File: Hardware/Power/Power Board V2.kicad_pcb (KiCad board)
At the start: 2 copper layers, 71.1 x 58.4 mm, 90 parts, among them IC1 LM3481MM, IC2 BP1360, IC3 DIO6912, IC4 BP1360, IC5 DIO6912, J1 Conn_01x02, J2 Conn_01x02, J3 Conn_01x02, J4 Conn_01x02, J5 Conn_02x05_Top_Bottom, Q1 2N7000, Q2 AO4264E, Q3 2N7000, Q4 PJM2301PSA-S

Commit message: KiCad Cleanup
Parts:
- added REF**: SOIC-8_3.9x4.9mm_P1.27mm, Package_SO:SOIC-8_3.9x4.9mm_P1.27mm, B.Cu at (168.8, 91.3)
- moved R5 3.03 mm to (110.7, 90.9), turned to 135 degrees
- moved R2 2.43 mm to (110.2, 83.2), turned to 0 degrees
- moved C8 2.13 mm to (110.2, 85.0), turned to 0 degrees
- moved R1 1.33 mm to (112.0, 89.7), turned to 135 degrees
- moved R6 0.44 mm to (112.4, 94.7)
- moved R4 0.40 mm to (113.8, 84.1)
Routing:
- net Net-(IC1-Pad8): track 17.5 -> 13.8 mm
- net Net-(Q2-Pad1): track 7.12 -> 3.82 mm
- net Net-(IC1-Pad2): track 21.4 -> 24.6 mm
- net Net-(C8-Pad1): track 18.2 -> 20.3 mm
- net GNDA: track 15.7 -> 14.7 mm, vias 55 -> 61
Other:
- board text added: "1"
- board text added: "Note: Pin 1 designator is longer line over pin"

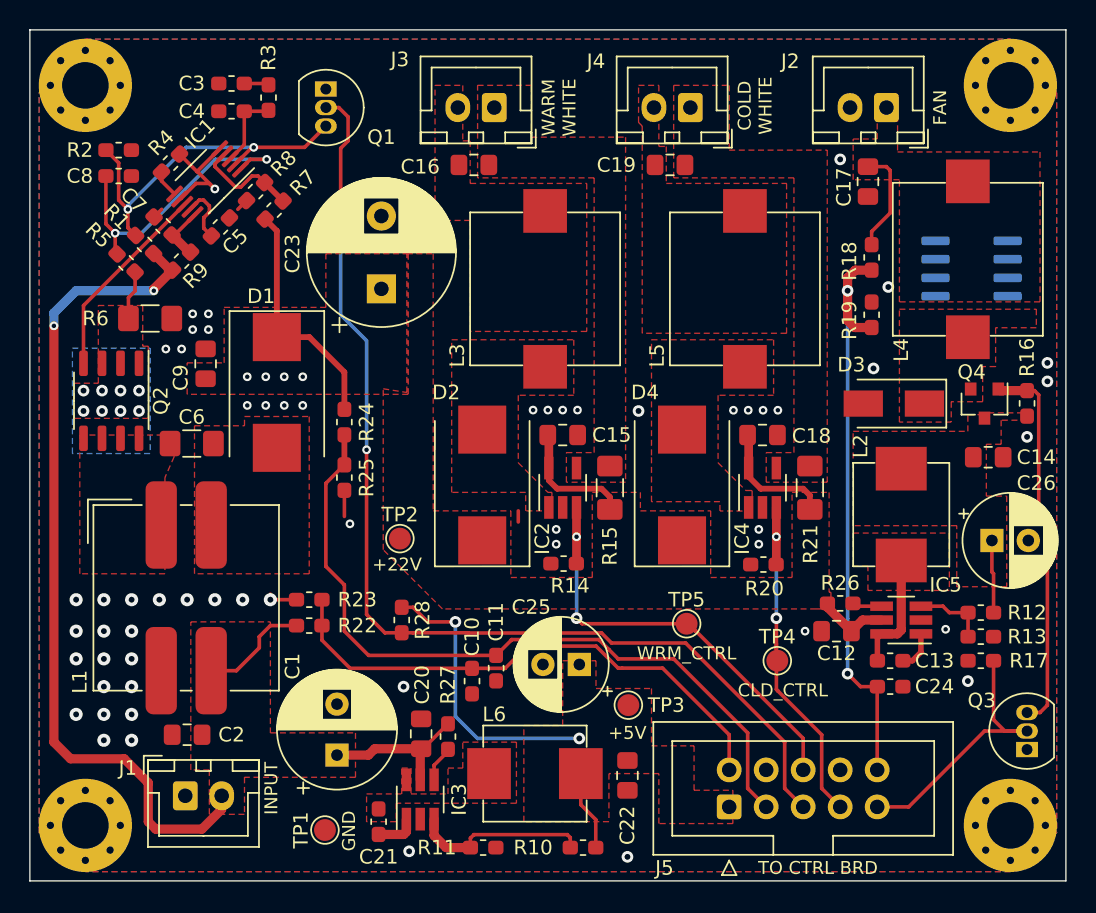
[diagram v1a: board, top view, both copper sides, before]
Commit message: Moved MCU Power Supply to Logic Board
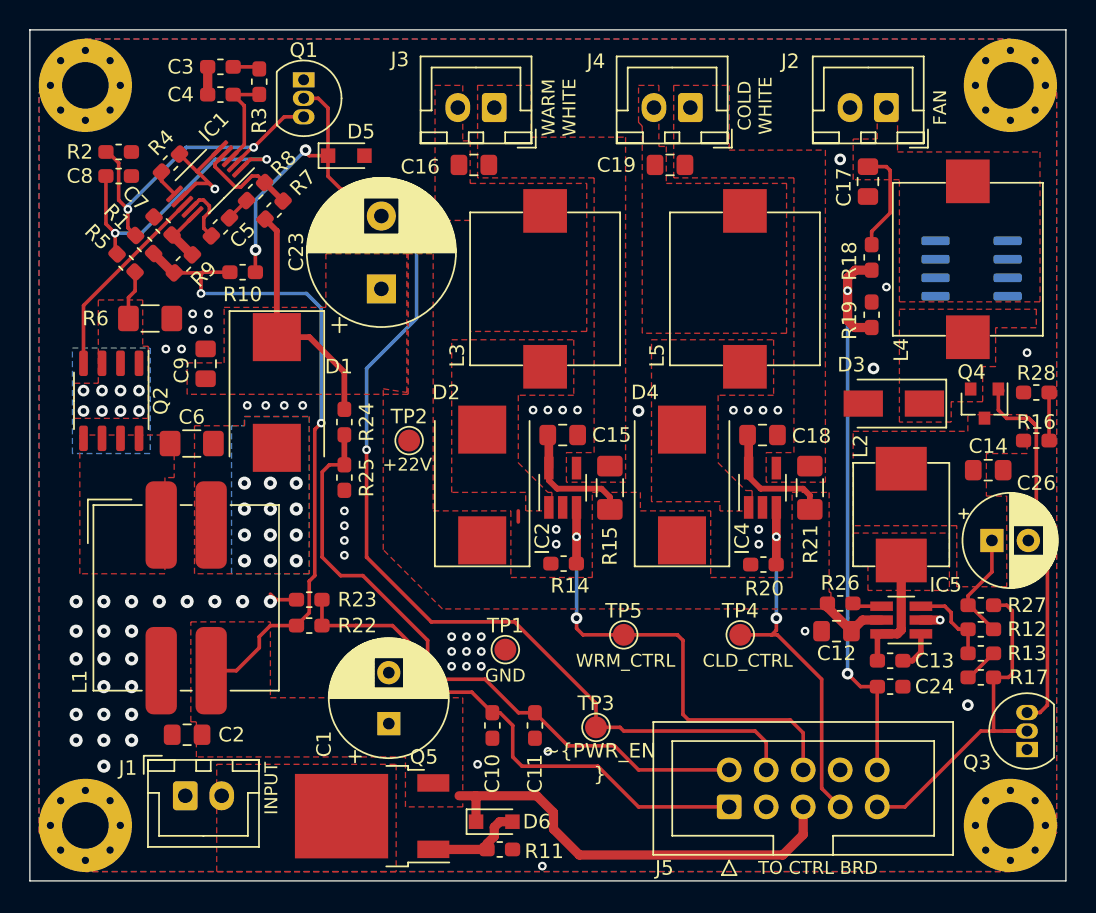
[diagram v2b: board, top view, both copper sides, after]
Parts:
- removed C20, C22: 2U2, Capacitor_SMD:C_0805_2012Metric_Pad1.15x1.40mm_HandSolder
- removed C21: 100N, Capacitor_SMD:C_0603_1608Metric_Pad1.05x0.95mm_HandSolder
- removed C25: CP, Capacitor_THT:CP_Radial_D6.3mm_P2.50mm
- removed IC3: DIO6912, Package_TO_SOT_SMD:SOT-23-6_Handsoldering
- removed L6: 22U, ArduinoLamp:YT0630
- added D5: D_Zener, Diode_SMD:D_SOD-323_HandSoldering, F.Cu at (125.9, 83.6)
- added D6: D_Zener, Diode_SMD:D_SOD-323_HandSoldering, F.Cu at (136.0, 129.3)
- added Q5: SUD08P06-155L, Package_TO_SOT_SMD:TO-252-2, F.Cu at (127.6, 128.9)
- R10: value 8K45 -> 25K5
- R11: value 1K15 -> R
- R17: value 105K -> 25K5
- TP3: value +5V -> ~PWR_EN
- moved R28 46.3 mm to (173.2, 99.8), turned to 180 degrees
- moved R10 45.9 mm to (118.7, 91.6), turned to 0 degrees
- moved R27 37.7 mm to (169.4, 114.4), turned to 0 degrees
- moved TP1 17.5 mm to (136.8, 117.5), turned to 0 degrees
- moved TP2 6.76 mm to (130.2, 103.1)
- moved C11 4.76 mm to (138.8, 122.7)
- moved TP5 4.38 mm to (144.9, 116.5)
- moved C1 4.16 mm to (128.8, 122.6)
- moved C10 3.35 mm to (135.9, 122.7)
- moved TP4 3.10 mm to (152.9, 116.5)
- moved TP3 2.69 mm to (143.0, 122.8), turned to 0 degrees
- moved R16 2.63 mm to (173.2, 103.1), turned to 0 degrees
- moved Q1 1.65 mm to (122.9, 78.4)
- moved C3 1.37 mm to (117.2, 77.5)
- moved C4 1.37 mm to (117.2, 79.4)
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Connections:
- C1 pad 1: VIN -> VIN_PROTECT
- C1 pad 2: GNDA -> GNDPWR
- C10 pad 2: GNDA -> GNDPWR
- C11 pad 2: GNDA -> GNDPWR
- C12 pad 2: GNDA -> GNDPWR
- C14 pad 2: GNDA -> GNDPWR
- C15 pad 2: GNDA -> GNDPWR
- C17 pad 2: GNDA -> GNDPWR
- C18 pad 2: GNDA -> GNDPWR
- C2 pad 1: VIN -> VIN_PROTECT
- C2 pad 2: GNDA -> GNDPWR
- C23 pad 2: GNDA -> GNDPWR
- C24 pad 2: GNDA -> GNDPWR
- C26 pad 2: GNDA -> GNDPWR
- C3 pad 2: GNDA -> GNDPWR
- C4 pad 2: GNDA -> GNDPWR
- C5 pad 2: GNDA -> GNDPWR
- C7 pad 2: GNDA -> GNDPWR
- C8 pad 2: GNDA -> GNDPWR
- C9 pad 2: GNDA -> GNDPWR
- D3 pad 2: GNDA -> GNDPWR
- H1 pad 1: GNDA -> GNDPWR
- H2 pad 1: GNDA -> GNDPWR
- H3 pad 1: GNDA -> GNDPWR
- H4 pad 1: GNDA -> GNDPWR
- IC1 pad 5: GNDA -> GNDPWR
- IC1 pad 7: GNDA -> GNDPWR
- IC2 pad 2: GNDA -> GNDPWR
- IC4 pad 2: GNDA -> GNDPWR
- IC5 pad 2: GNDA -> GNDPWR
- J1 pad 1: GNDA -> GNDPWR
- J1 pad 2: VIN -> /Reverse Input Protection/VIN
- J2 pad 2: GNDA -> GNDPWR
- J5 pad 1: +5V -> VIN_FB
- J5 pad 2: VIN_FB -> VOUT_FB
- J5 pad 3: VOUT_FB -> GNDPWR
- J5 pad 4: GNDA -> ~PWR_EN
- J5 pad 5: PWR_EN -> VIN_PROTECT
- J5 pad 8: GNDA -> GNDPWR
- L1 pad 3: VIN -> VIN_PROTECT
- L1 pad 4: GNDA -> GNDPWR
- Q1 pad 1: GNDA -> GNDPWR
- Q1 pad 2: PWR_EN -> ~PWR_EN
- Q3 pad 1: GNDA -> GNDPWR
- R1 pad 1: VIN -> VIN_PROTECT
- R10 pad 1: +5V -> VIN_PROTECT
- R10 pad 2: /Logic Power Supply/FB -> ~PWR_EN
- R11 pad 1: /Logic Power Supply/FB -> Net-(D6-Pad2)
- R11 pad 2: GNDA -> GNDPWR
- R13 pad 2: GNDA -> GNDPWR
- R14 pad 2: GNDA -> GNDPWR
- R16 pad 2: Net-(Q3-Pad3) -> Net-(R16-Pad2)
- R17 pad 2: GNDA -> GNDPWR
- R19 pad 2: GNDA -> GNDPWR
- R2 pad 2: GNDA -> GNDPWR
- R20 pad 2: GNDA -> GNDPWR
- R22 pad 1: VIN -> VIN_PROTECT
- R23 pad 2: GNDA -> GNDPWR
- R25 pad 2: GNDA -> GNDPWR
- R27 pad 1: VIN -> /+13V9
- R27 pad 2: Net-(IC3-Pad4) -> FAN_CTRL
- R28 pad 1: +5V -> Net-(R16-Pad2)
- R28 pad 2: PWR_EN -> GNDPWR
- R4 pad 2: GNDA -> GNDPWR
- R6 pad 2: GNDA -> GNDPWR
- R8 pad 2: GNDA -> GNDPWR
- R9 pad 1: VIN -> VIN_PROTECT
- TP1 pad 1: GNDA -> GNDPWR
- TP3 pad 1: +5V -> ~PWR_EN
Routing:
- net ~PWR_EN: track 0.00 -> 86.6 mm, vias 0 -> 4
- net VIN_PROTECT: track 0.00 -> 76.5 mm, vias 0 -> 2
- net VIN: track 76.0 -> 0.00 mm, vias 2 -> 0
- net PWR_EN: track 74.2 -> 0.00 mm, vias 2 -> 0
- net +5V: track 24.8 -> 0.00 mm, vias 2 -> 0
- net GNDPWR: track 0.00 -> 17.9 mm, vias 0 -> 70
- net GNDA: track 14.7 -> 0.76 mm, vias 61 -> 0
- net /Logic Power Supply/FB: track 12.3 -> 0.00 mm
- net Net-(D6-Pad2): track 0.00 -> 7.00 mm
- net VOUT_FB: track 51.6 -> 45.0 mm
- net FAN_CTRL: track 19.1 -> 24.8 mm
- net YELLOW_CTRL: track 30.6 -> 34.2 mm
- net Net-(R16-Pad2): track 0.00 -> 3.30 mm
- net Net-(C21-Pad1): track 2.85 -> 0.00 mm
- net /+13V9: track 5.00 -> 7.56 mm
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- added copper zone on F.Cu, net /Reverse Input Protection/VIN
- added copper zone on B.Cu, net GNDPWR
- added copper zone on F.Cu, net GNDPWR
- added copper zone on B.Cu, net Net-(C6-Pad2)
- added copper zone on F.Cu, net VIN_PROTECT
- removed copper zone on F.Cu, net +5V
- removed copper zone on B.Cu, net GNDA
- removed copper zone on F.Cu, net GNDA
- removed copper zone on F.Cu, net Net-(C21-Pad2)
- removed copper zone on F.Cu, net VIN
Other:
- board text added: "~PWR_EN"
- board text removed: "+5V"

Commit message: Removed Logic Board PSU from Power Board
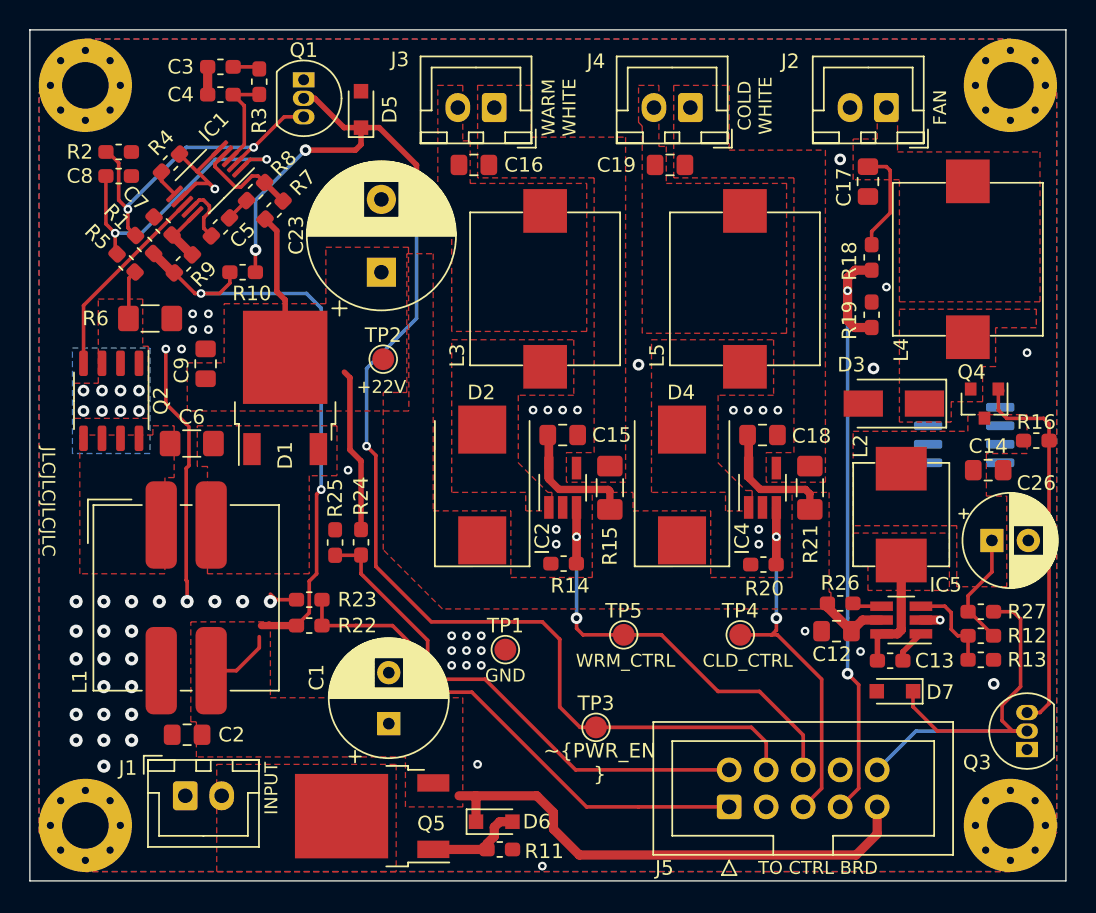
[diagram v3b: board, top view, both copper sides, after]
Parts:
- removed C10, C11, C24: 100N, Capacitor_SMD:C_0603_1608Metric_Pad1.05x0.95mm_HandSolder
- removed R17, R28: 25K5, Resistor_SMD:R_0603_1608Metric_Pad1.05x0.95mm_HandSolder
- added D7: D_Zener, Diode_SMD:D_SOD-323_HandSoldering, F.Cu at (163.5, 120.3)
- C3: value 1N2 -> 330N
- C4: value 330N -> 1N2
- D1: value SS510 -> MBRD5100; footprint ArduinoLamp:D_SMC_Handsoldering_Shortened -> ArduinoLamp:TO-252-2_ConnectedPins
- J1: value Conn_01x02 -> Power Input
- J2: value Conn_01x02 -> Fan
- J3: value Conn_01x02 -> Cold White LED
- J4: value Conn_01x02 -> Warm White LED
- J5: value Conn_02x05_Top_Bottom -> Logic Board
- R11: value R -> 25K5
- moved G*** 15.2 mm to (145.0, 113.0)
- moved REF** 11.4 mm to (168.3, 102.7)
- moved R24 8.33 mm to (126.9, 110.1)
- moved TP2 5.86 mm to (128.4, 97.5)
- moved R25 4.50 mm to (125.1, 110.1), turned to 90 degrees
- moved D5 3.33 mm to (126.9, 80.4), turned to 90 degrees
- moved REF** 2.38 mm to (119.9, 119.6)
- moved C23 1.14 mm to (128.3, 91.6)
- moved D1 0.65 mm to (121.7, 99.5), turned to 90 degrees
- moved R13 0.44 mm to (169.4, 118.2)
- moved R12 0.44 mm to (169.4, 116.5)
- moved R27 0.44 mm to (169.4, 114.9)
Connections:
- net /+13V9 renamed /PWM Fan Control/VIN
- net /+22V renamed +22V
- J5 pad 10: FAN_FB -> FAN_CTRL
- J5 pad 5: VIN_PROTECT -> BLUE_CTRL
- J5 pad 7: BLUE_CTRL -> FAN_FB
- J5 pad 9: FAN_CTRL -> VIN_PROTECT
- R16 pad 2: Net-(R16-Pad2) -> Net-(Q3-Pad3)
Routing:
- net GNDPWR: track 17.9 -> 33.4 mm, vias 70 -> 63
- net VOUT_FB: track 45.0 -> 35.3 mm
- net FAN_CTRL: track 24.8 -> 32.5 mm
- net +22V: track 38.8 -> 44.5 mm
- net VIN_PROTECT: track 76.5 -> 81.2 mm
- net ~PWR_EN: track 86.6 -> 90.4 mm
- net Net-(R16-Pad2): track 3.30 -> 0.00 mm
- net YELLOW_CTRL: track 34.2 -> 31.2 mm
- net FAN_FB: track 41.1 -> 42.9 mm
- net VIN_FB: track 37.7 -> 36.4 mm
- net GNDA: track 0.76 -> 0.00 mm
- net Net-(C6-Pad2): vias 12 -> 0
- removed copper zone on B.Cu, net Net-(C6-Pad2)
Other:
- rule trace_min: 0.1524 -> 0.2032
- board text added: "INPUT PASSTHROUGH 800mA MAX"
- board text added: "JLCJLCJLCJLC"
- board text removed: "LOGIC 5VDC \ 750mA"

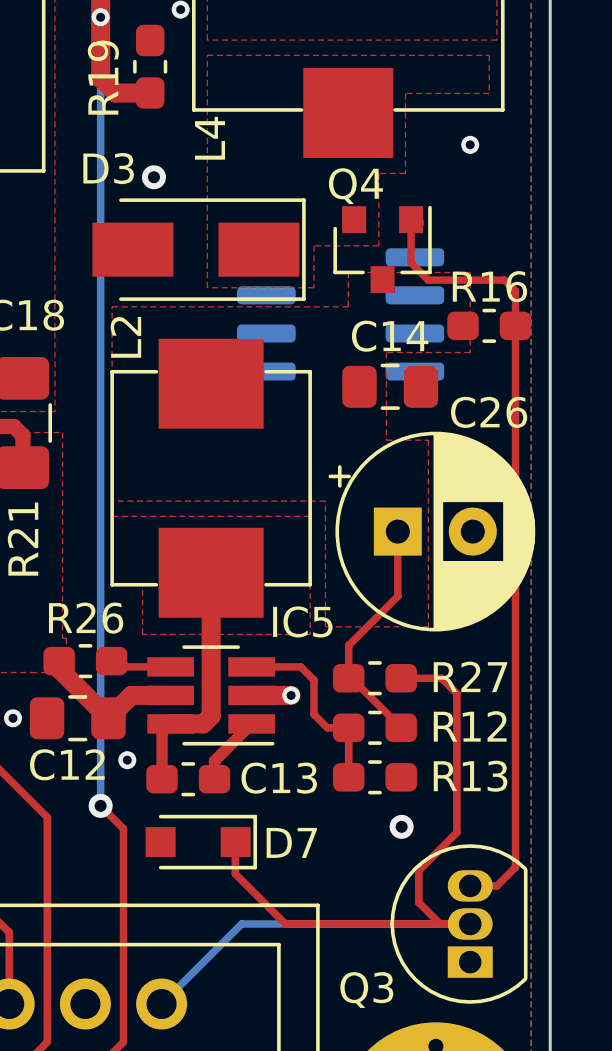
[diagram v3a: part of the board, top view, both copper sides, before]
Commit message: Fixed Power Board Errata
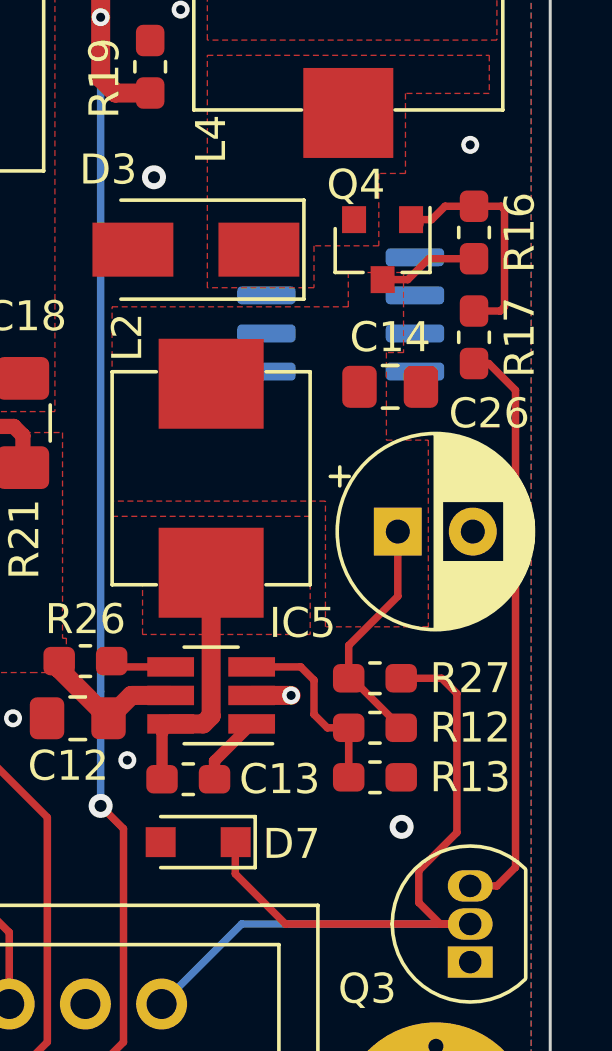
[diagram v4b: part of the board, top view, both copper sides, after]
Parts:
- added R17: 2K2, Resistor_SMD:R_0603_1608Metric_Pad1.05x0.95mm_HandSolder, F.Cu at (172.7, 103.5)
- R16: value 105K -> 1K15
- moved R16 3.15 mm to (172.7, 100.0), turned to 90 degrees
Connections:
- C17 pad 2: GNDPWR -> Net-(C17-Pad2)
- Q4 pad 1: Net-(Q3-Pad3) -> Net-(Q4-Pad1)
- R16 pad 2: Net-(Q3-Pad3) -> Net-(Q4-Pad1)
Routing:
- net Net-(Q4-Pad1): track 0.00 -> 7.82 mm
- net Net-(Q3-Pad3): track 26.4 -> 19.4 mm
- net /PWM Fan Control/VIN: track 7.46 -> 10.8 mm
